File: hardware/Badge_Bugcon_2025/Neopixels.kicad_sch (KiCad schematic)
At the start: 11 parts

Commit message: feat(Hw):Update_Schematic_And_Floorplan
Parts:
- C2, C21, C43, C46, C47: footprint Capacitor_SMD:C_0603_1608Metric -> Capacitor_SMD:C_0402_1005Metric; LCSC# C338117 -> C77020
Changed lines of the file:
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@@
 			)
 		)
-		(property "Footprint" "Capacitor_SMD:C_0603_1608Metric"
+		(property "Footprint" "Capacitor_SMD:C_0402_1005Metric"
 			(at 127 54.61 0)
 			(effects
@@
 			)
 		)
-		(property "LCSC#" "C338117"
+		(property "LCSC#" "C77020"
 			(at 127 54.61 0)
 			(effects
@@
 			)
 		)
-		(property "Footprint" "Capacitor_SMD:C_0603_1608Metric"
+		(property "Footprint" "Capacitor_SMD:C_0402_1005Metric"
 			(at 105.41 54.61 0)
 			(effects
@@
 			)
 		)
-		(property "LCSC#" "C338117"
+		(property "LCSC#" "C77020"
 			(at 105.41 54.61 0)
 			(effects
@@
 			)
 		)
-		(property "Footprint" "Capacitor_SMD:C_0603_1608Metric"
+		(property "Footprint" "Capacitor_SMD:C_0402_1005Metric"
 			(at 153.67 54.61 0)
 			(effects
@@
 			)
 		)
-		(property "LCSC#" "C338117"
+		(property "LCSC#" "C77020"
 			(at 153.67 54.61 0)
 			(effects
@@
 			)
 		)
-		(property "Footprint" "Capacitor_SMD:C_0603_1608Metric"
+		(property "Footprint" "Capacitor_SMD:C_0402_1005Metric"
 			(at 85.09 54.61 0)
 			(effects
@@
 			)
 		)
-		(property "LCSC#" "C338117"
+		(property "LCSC#" "C77020"
 			(at 85.09 54.61 0)
 			(effects
@@
 			)
 		)
-		(property "Footprint" "Capacitor_SMD:C_0603_1608Metric"
+		(property "Footprint" "Capacitor_SMD:C_0402_1005Metric"
 			(at 63.5 54.61 0)
 			(effects
@@
 			)
 		)
-		(property "LCSC#" "C338117"
+		(property "LCSC#" "C77020"
 			(at 63.5 54.61 0)
 			(effects

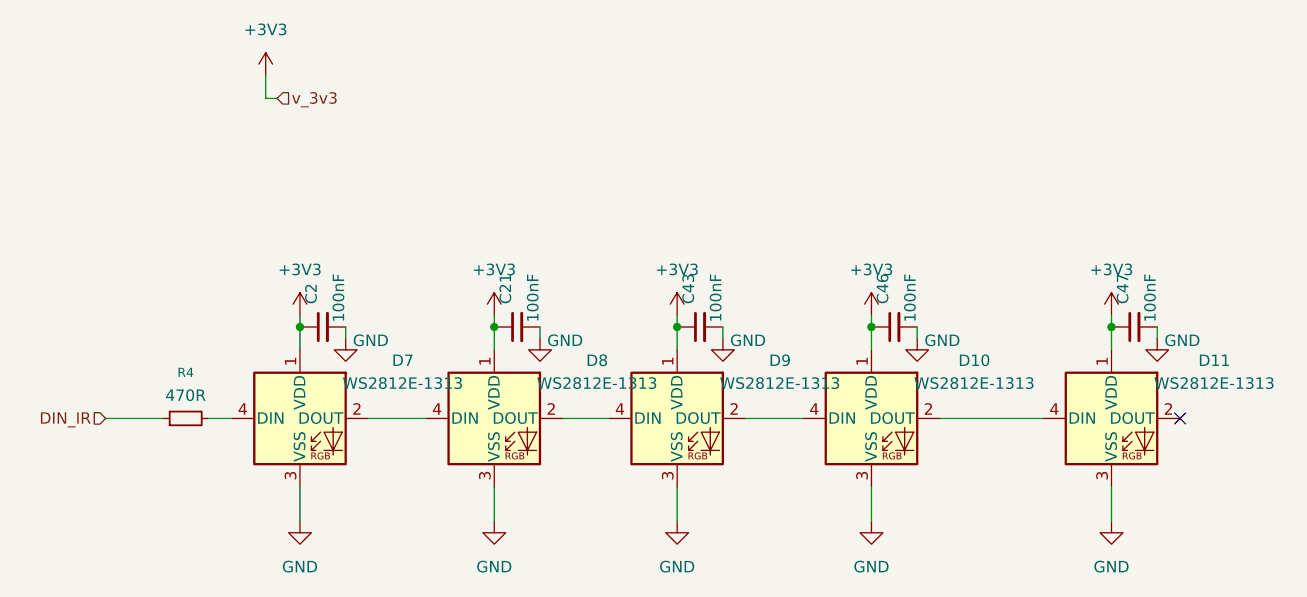
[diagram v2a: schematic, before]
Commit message: feat(Hw):Update_Schematic_And_Floorplan
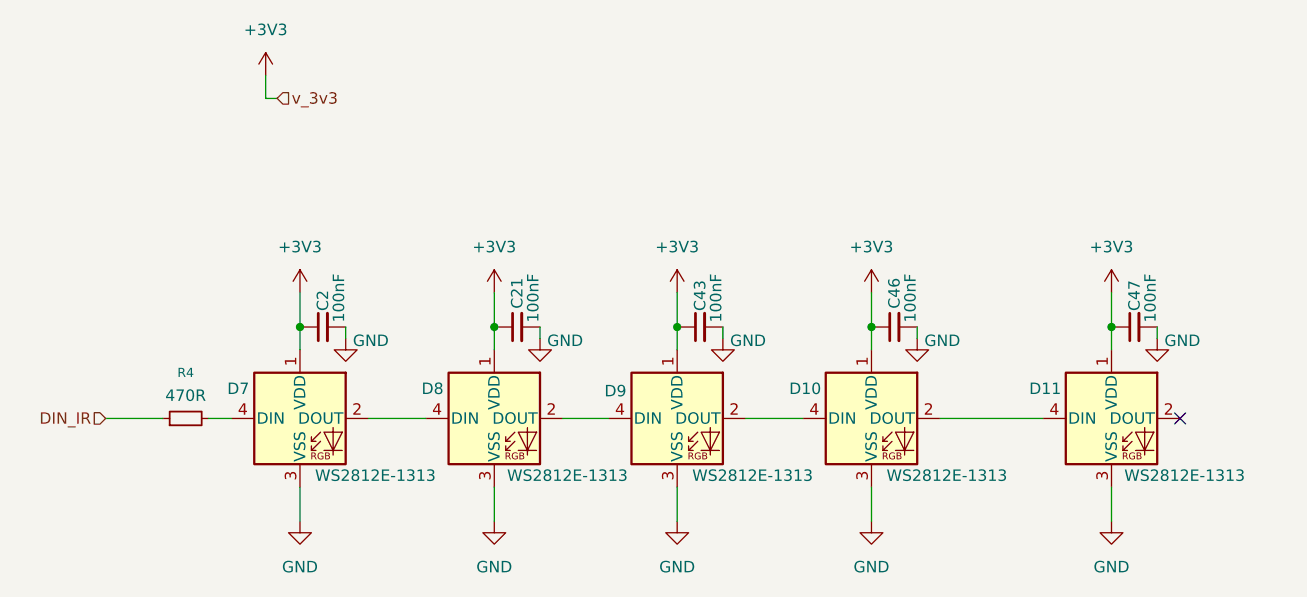
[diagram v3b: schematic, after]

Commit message: feat(Hw):Update_Schematic
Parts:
- removed C21, C43, C46, C47: 100nF, Capacitor_SMD:C_0402_1005Metric, symbol Device:C_Small
- removed D10, D11, D8, D9: WS2812E-1313, Footprints:WS2812E-1313, symbol LED:WS2812B

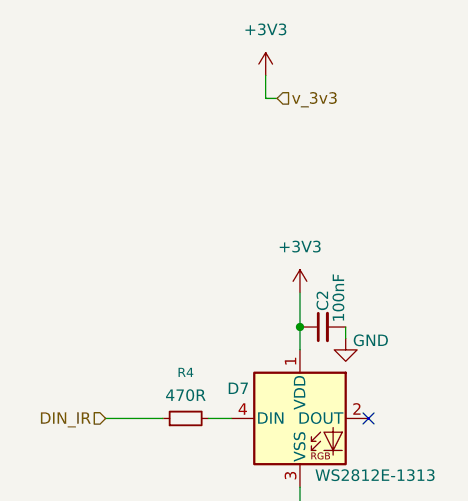
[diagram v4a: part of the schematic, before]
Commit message: feat(Hw):Update_Schaematic_And_BOM
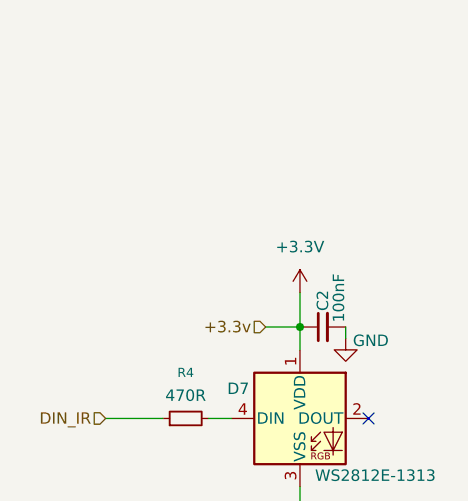
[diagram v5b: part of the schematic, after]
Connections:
- net +3V3 renamed +3.3V
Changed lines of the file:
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@@
 	(wire
 		(pts
-			(xy 57.15 26.67) (xy 57.15 29.21)
+			(xy 39.37 64.77) (xy 45.72 64.77)
 		)
 		(stroke
@@
 	(wire
 		(pts
-			(xy 57.15 29.21) (xy 58.42 29.21)
-		)
-		(stroke
-			(width 0)
-			(type default)
-		)
-	)
-	(wire
-		(pts
-			(xy 39.37 64.77) (xy 45.72 64.77)
+			(xy 57.15 54.61) (xy 60.96 54.61)
 		)
 		(stroke
@@
 		)
 	)
-	(hierarchical_label "v_3v3"
+	(hierarchical_label "+3.3v"
 		(shape input)
-		(at 58.42 29.21 0)
+		(at 57.15 54.61 180)
 		(effects
 			(font
 				(size 1.27 1.27)
 			)
-			(justify left)
+			(justify right)
 		)
 	)
@@
 			)
 			(justify right)
-		)
-	)
-	(symbol
-		(lib_id "power:+3V3")
-		(at 57.15 26.67 0)
-		(unit 1)
-		(exclude_from_sim no)
-		(in_bom yes)
-		(on_board yes)
-		(dnp no)
-		(fields_autoplaced yes)
-		(property "Reference" "#PWR089"
-			(at 57.15 30.48 0)
-			(effects
-				(font
-					(size 1.27 1.27)
-				)
-				(hide yes)
-			)
-		)
-		(property "Value" "+3V3"
-			(at 57.15 21.59 0)
-			(effects
-				(font
-					(size 1.27 1.27)
-				)
-			)
-		)
-		(property "Footprint" ""
-			(at 57.15 26.67 0)
-			(effects
-				(font
-					(size 1.27 1.27)
-				)
-				(hide yes)
-			)
-		)
-		(property "Datasheet" ""
-			(at 57.15 26.67 0)
-			(effects
-				(font
-					(size 1.27 1.27)
-				)
-				(hide yes)
-			)
-		)
-		(property "Description" "Power symbol creates a global label with name \"+3V3\""
-			(at 57.15 26.67 0)
-			(effects
-				(font
-					(size 1.27 1.27)
-				)
-				(hide yes)
-			)
-		)
-		(pin "1"
-		)
-		(instances
-			(project "Badge_Bugcon_2025"
-				(path "/a95785a0-0aa1-454e-b59f-0ac64970ac71/680de73f-0f07-4b07-a85f-a6661c323846"
-					(reference "#PWR089")
-					(unit 1)
-				)
-			)
 		)
 	)
@@
 				(path "/a95785a0-0aa1-454e-b59f-0ac64970ac71/680de73f-0f07-4b07-a85f-a6661c323846"
 					(reference "#PWR0115")
-					(unit 1)
-				)
-			)
-		)
-	)
-	(symbol
-		(lib_id "power:+3V3")
-		(at 60.96 50.8 0)
-		(unit 1)
-		(exclude_from_sim no)
-		(in_bom yes)
-		(on_board yes)
-		(dnp no)
-		(fields_autoplaced yes)
-		(property "Reference" "#PWR0117"
-			(at 60.96 54.61 0)
-			(effects
-				(font
-					(size 1.27 1.27)
-				)
-				(hide yes)
-			)
-		)
-		(property "Value" "+3V3"
-			(at 60.96 45.72 0)
-			(effects
-				(font
-					(size 1.27 1.27)
-				)
-			)
-		)
-		(property "Footprint" ""
-			(at 60.96 50.8 0)
-			(effects
-				(font
-					(size 1.27 1.27)
-				)
-				(hide yes)
-			)
-		)
-		(property "Datasheet" ""
-			(at 60.96 50.8 0)
-			(effects
-				(font
-					(size 1.27 1.27)
-				)
-				(hide yes)
-			)
-		)
-		(property "Description" "Power symbol creates a global label with name \"+3V3\""
-			(at 60.96 50.8 0)
-			(effects
-				(font
-					(size 1.27 1.27)
-				)
-				(hide yes)
-			)
-		)
-		(pin "1"
-		)
-		(instances
-			(project "Badge_Bugcon_2025"
-				(path "/a95785a0-0aa1-454e-b59f-0ac64970ac71/680de73f-0f07-4b07-a85f-a6661c323846"
-					(reference "#PWR0117")
 					(unit 1)
 				)
@@
 			)
 		)
+		(property "JLCPCB" ""
+			(at 48.26 64.77 90)
+			(effects
+				(font
+					(size 1.27 1.27)
+				)
+				(hide yes)
+			)
+		)
+		(property "Manufacter Number" ""
+			(at 48.26 64.77 90)
+			(effects
+				(font
+					(size 1.27 1.27)
+				)
+				(hide yes)
+			)
+		)
 		(pin "1"
 		)
@@
 			)
 		)
+		(property "JLCPCB" ""
+			(at 60.96 64.77 0)
+			(effects
+				(font
+					(size 1.27 1.27)
+				)
+				(hide yes)
+			)
+		)
+		(property "Manufacter Number" ""
+			(at 60.96 64.77 0)
+			(effects
+				(font
+					(size 1.27 1.27)
+				)
+				(hide yes)
+			)
+		)
 		(pin "2"
 		)
@@
 				(path "/a95785a0-0aa1-454e-b59f-0ac64970ac71/680de73f-0f07-4b07-a85f-a6661c323846"
 					(reference "D7")
+					(unit 1)
+				)
+			)
+		)
+	)
+	(symbol
+		(lib_id "power:+3.3V")
+		(at 60.96 50.8 0)
+		(unit 1)
+		(exclude_from_sim no)
+		(in_bom yes)
+		(on_board yes)
+		(dnp no)
+		(fields_autoplaced yes)
+		(property "Reference" "#PWR0101"
+			(at 60.96 54.61 0)
+			(effects
+				(font
+					(size 1.27 1.27)
+				)
+				(hide yes)
+			)
+		)
+		(property "Value" "+3.3V"
+			(at 60.96 45.72 0)
+			(effects
+				(font
+					(size 1.27 1.27)
+				)
+			)
+		)
+		(property "Footprint" ""
+			(at 60.96 50.8 0)
+			(effects
+				(font
+					(size 1.27 1.27)
+				)
+				(hide yes)
+			)
+		)
+		(property "Datasheet" ""
+			(at 60.96 50.8 0)
+			(effects
+				(font
+					(size 1.27 1.27)
+				)
+				(hide yes)
+			)
+		)
+		(property "Description" "Power symbol creates a global label with name \"+3.3V\""
+			(at 60.96 50.8 0)
+			(effects
+				(font
+					(size 1.27 1.27)
+				)
+				(hide yes)
+			)
+		)
+		(pin "1"
+		)
+		(instances
+			(project "Badge_Bugcon_2025"
+				(path "/a95785a0-0aa1-454e-b59f-0ac64970ac71/680de73f-0f07-4b07-a85f-a6661c323846"
+					(reference "#PWR0101")
 					(unit 1)
 				)
@@
 			(at 63.5 54.61 0)
 			(effects
+				(font
+					(size 1.27 1.27)
+				)
+				(hide yes)
+			)
+		)
+		(property "JLCPCB" ""
+			(at 63.5 54.61 0)
+			(effects
+				(font
+					(size 1.27 1.27)
+				)
+				(hide yes)
+			)
+		)
+		(property "Manufacter Number" ""
+			(at 63.5 54.61 0)
+			(effects
